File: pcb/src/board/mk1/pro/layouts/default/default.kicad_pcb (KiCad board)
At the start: 2 copper layers, 256 parts

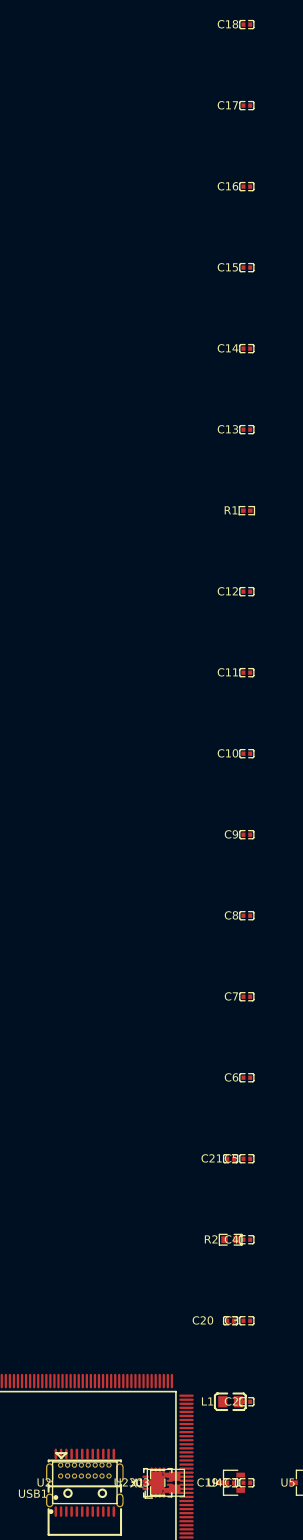
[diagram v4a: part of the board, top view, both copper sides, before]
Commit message: pcb: add decoupling capacitors to STM32F429
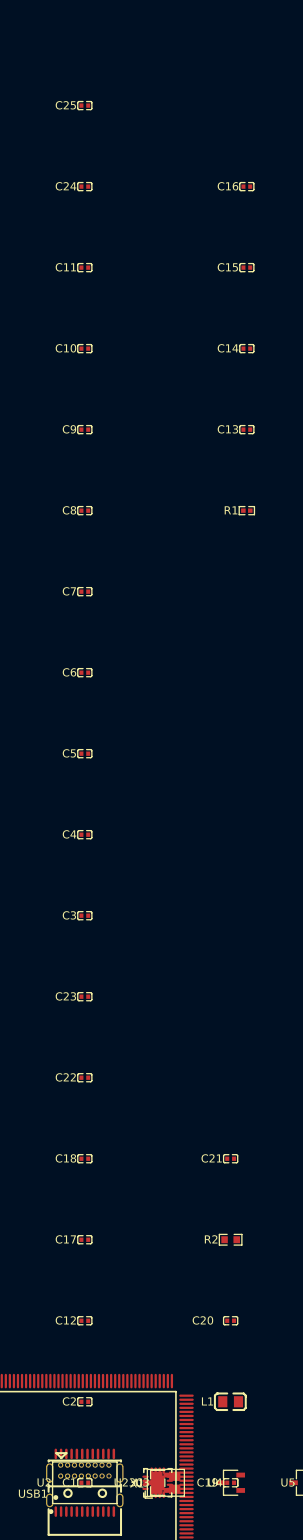
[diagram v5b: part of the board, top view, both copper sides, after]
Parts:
- added C22: 100nF ±10%, Samsung_Electro_Mechanics_CL05B104KO5NNNC:C0402, F.Cu at (0.00, -50.0)
- added C23: 100nF ±10%, Samsung_Electro_Mechanics_CL05B104KO5NNNC:C0402, F.Cu at (0.00, -60.0)
- added C24: 1µF ±10%, Samsung_Electro_Mechanics_CL05A105KA5NQNC:C0402, F.Cu at (0.00, -160.0)
- added C25: 10nF ±10%, Samsung_Electro_Mechanics_CL05B103KB5NNNC:C0402, F.Cu at (0.00, -170.0)
- C1: value 100nF ±10% -> 4.7µF ±20%; footprint Samsung_Electro_Mechanics_CL05B104KO5NNNC:C0402 -> Samsung_Electro_Mechanics_CL05A475MP5NRNC:C0402
- C17: value 1µF ±10% -> 100nF ±10%; footprint Samsung_Electro_Mechanics_CL05A105KA5NQNC:C0402 -> Samsung_Electro_Mechanics_CL05B104KO5NNNC:C0402
- moved C17 141.4 mm to (0.00, -30.0)
- moved C18 141.4 mm to (0.00, -40.0)
- moved C12 92.2 mm to (0.00, -20.0)
- moved C10 53.9 mm to (0.00, -140.0)
- moved C11 53.9 mm to (0.00, -150.0)
- moved C3 53.9 mm to (0.00, -70.0)
- moved C4 53.9 mm to (0.00, -80.0)
- moved C5 53.9 mm to (0.00, -90.0)
- moved C6 53.9 mm to (0.00, -100.0)
- moved C7 53.9 mm to (0.00, -110.0)
- moved C8 53.9 mm to (0.00, -120.0)
- moved C9 53.9 mm to (0.00, -130.0)
- moved C1 20.0 mm to (0.00, 0.00)
- moved C2 20.0 mm to (0.00, -10.0)
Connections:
- C1 pad 1: vref_caps[1]-power-hv -> out_cap-power-hv
- C10 pad 1: vref_caps[1]-power-hv -> out_cap-power-hv
- C11 pad 1: vref_caps[1]-power-hv -> out_cap-power-hv
- C12 pad 1: vref_caps[1]-power-hv -> out_cap-power-hv
- C15 pad 1: vcap_caps[1]-power-hv -> vcap_caps[0]-power-hv
- C17 pad 1: vref_caps[1]-power-hv -> out_cap-power-hv
- C18 pad 1: vref_caps[1]-power-hv -> out_cap-power-hv
- C2 pad 1: vref_caps[1]-power-hv -> out_cap-power-hv
- C20 pad 1: vref_caps[1]-power-hv -> out_cap-power-hv
- C3 pad 1: vref_caps[1]-power-hv -> out_cap-power-hv
- C4 pad 1: vref_caps[1]-power-hv -> out_cap-power-hv
- C5 pad 1: vref_caps[1]-power-hv -> out_cap-power-hv
- C6 pad 1: vref_caps[1]-power-hv -> out_cap-power-hv
- C7 pad 1: vref_caps[1]-power-hv -> out_cap-power-hv
- C8 pad 1: vref_caps[1]-power-hv -> out_cap-power-hv
- C9 pad 1: vref_caps[1]-power-hv -> out_cap-power-hv
- L1 pad 2: vref_caps[1]-power-hv -> out_cap-power-hv
- R2 pad 1: vref_caps[1]-power-hv -> out_cap-power-hv
- U1 pad 103: vref_caps[1]-power-hv -> out_cap-power-hv
- U1 pad 114: vref_caps[1]-power-hv -> out_cap-power-hv
- U1 pad 125: 125 -> vcap_caps[1]-power-hv
- U1 pad 127: vref_caps[1]-power-hv -> out_cap-power-hv
- U1 pad 136: vref_caps[1]-power-hv -> out_cap-power-hv
- U1 pad 149: vref_caps[1]-power-hv -> out_cap-power-hv
- U1 pad 15: vref_caps[1]-power-hv -> out_cap-power-hv
- U1 pad 159: vref_caps[1]-power-hv -> out_cap-power-hv
- U1 pad 172: vref_caps[1]-power-hv -> out_cap-power-hv
- U1 pad 23: vref_caps[1]-power-hv -> out_cap-power-hv
- U1 pad 36: vref_caps[1]-power-hv -> out_cap-power-hv
- U1 pad 38: vref_caps[1]-power-hv -> out_cap-power-hv
- U1 pad 39: vref_caps[1]-power-hv -> out_cap-power-hv
- U1 pad 49: vref_caps[1]-power-hv -> out_cap-power-hv
- U1 pad 6: vbat-hv -> out_cap-power-hv
- U1 pad 62: vref_caps[1]-power-hv -> out_cap-power-hv
- U1 pad 72: vref_caps[1]-power-hv -> out_cap-power-hv
- U1 pad 81: vcap_caps[1]-power-hv -> vcap_caps[0]-power-hv
- U1 pad 82: vref_caps[1]-power-hv -> out_cap-power-hv
- U1 pad 91: vref_caps[1]-power-hv -> out_cap-power-hv
- U10 pad 1: vref_caps[1]-power-hv -> out_cap-power-hv
- U100 pad 1: vref_caps[1]-power-hv -> out_cap-power-hv
- U101 pad 1: vref_caps[1]-power-hv -> out_cap-power-hv
- U102 pad 1: vref_caps[1]-power-hv -> out_cap-power-hv
- U103 pad 1: vref_caps[1]-power-hv -> out_cap-power-hv
- U104 pad 1: vref_caps[1]-power-hv -> out_cap-power-hv
- U105 pad 1: vref_caps[1]-power-hv -> out_cap-power-hv
- U106 pad 1: vref_caps[1]-power-hv -> out_cap-power-hv
- U107 pad 1: vref_caps[1]-power-hv -> out_cap-power-hv
- U108 pad 1: vref_caps[1]-power-hv -> out_cap-power-hv
- U109 pad 1: vref_caps[1]-power-hv -> out_cap-power-hv
- U11 pad 1: vref_caps[1]-power-hv -> out_cap-power-hv
- U110 pad 24: vref_caps[1]-power-hv -> out_cap-power-hv
- U111 pad 1: vref_caps[1]-power-hv -> out_cap-power-hv
- U112 pad 1: vref_caps[1]-power-hv -> out_cap-power-hv
- U113 pad 1: vref_caps[1]-power-hv -> out_cap-power-hv
- U114 pad 1: vref_caps[1]-power-hv -> out_cap-power-hv
- U115 pad 1: vref_caps[1]-power-hv -> out_cap-power-hv
- U116 pad 1: vref_caps[1]-power-hv -> out_cap-power-hv
- U117 pad 1: vref_caps[1]-power-hv -> out_cap-power-hv
- U118 pad 1: vref_caps[1]-power-hv -> out_cap-power-hv
- U119 pad 1: vref_caps[1]-power-hv -> out_cap-power-hv
- U12 pad 1: vref_caps[1]-power-hv -> out_cap-power-hv
- U120 pad 1: vref_caps[1]-power-hv -> out_cap-power-hv
- U121 pad 1: vref_caps[1]-power-hv -> out_cap-power-hv
- U122 pad 24: vref_caps[1]-power-hv -> out_cap-power-hv
- U123 pad 1: vref_caps[1]-power-hv -> out_cap-power-hv
- U124 pad 1: vref_caps[1]-power-hv -> out_cap-power-hv
- U125 pad 1: vref_caps[1]-power-hv -> out_cap-power-hv
- U126 pad 1: vref_caps[1]-power-hv -> out_cap-power-hv
- U127 pad 1: vref_caps[1]-power-hv -> out_cap-power-hv
- U128 pad 1: vref_caps[1]-power-hv -> out_cap-power-hv
- U129 pad 1: vref_caps[1]-power-hv -> out_cap-power-hv
- U13 pad 1: vref_caps[1]-power-hv -> out_cap-power-hv
- U130 pad 1: vref_caps[1]-power-hv -> out_cap-power-hv
- U131 pad 1: vref_caps[1]-power-hv -> out_cap-power-hv
- U132 pad 1: vref_caps[1]-power-hv -> out_cap-power-hv
- U133 pad 1: vref_caps[1]-power-hv -> out_cap-power-hv
- U134 pad 24: vref_caps[1]-power-hv -> out_cap-power-hv
- U135 pad 1: vref_caps[1]-power-hv -> out_cap-power-hv
- U136 pad 1: vref_caps[1]-power-hv -> out_cap-power-hv
- U137 pad 1: vref_caps[1]-power-hv -> out_cap-power-hv
- U138 pad 1: vref_caps[1]-power-hv -> out_cap-power-hv
- U139 pad 1: vref_caps[1]-power-hv -> out_cap-power-hv
- U14 pad 24: vref_caps[1]-power-hv -> out_cap-power-hv
- U140 pad 1: vref_caps[1]-power-hv -> out_cap-power-hv
- U141 pad 1: vref_caps[1]-power-hv -> out_cap-power-hv
- U142 pad 1: vref_caps[1]-power-hv -> out_cap-power-hv
- U143 pad 1: vref_caps[1]-power-hv -> out_cap-power-hv
- U144 pad 1: vref_caps[1]-power-hv -> out_cap-power-hv
- U145 pad 1: vref_caps[1]-power-hv -> out_cap-power-hv
- U146 pad 24: vref_caps[1]-power-hv -> out_cap-power-hv
- U147 pad 1: vref_caps[1]-power-hv -> out_cap-power-hv
- U148 pad 1: vref_caps[1]-power-hv -> out_cap-power-hv
- U149 pad 1: vref_caps[1]-power-hv -> out_cap-power-hv
- U15 pad 1: vref_caps[1]-power-hv -> out_cap-power-hv
- U150 pad 1: vref_caps[1]-power-hv -> out_cap-power-hv
- U151 pad 1: vref_caps[1]-power-hv -> out_cap-power-hv
- U152 pad 1: vref_caps[1]-power-hv -> out_cap-power-hv
- U153 pad 1: vref_caps[1]-power-hv -> out_cap-power-hv
- U154 pad 1: vref_caps[1]-power-hv -> out_cap-power-hv
- U155 pad 1: vref_caps[1]-power-hv -> out_cap-power-hv
- U156 pad 1: vref_caps[1]-power-hv -> out_cap-power-hv
- U157 pad 1: vref_caps[1]-power-hv -> out_cap-power-hv
- U158 pad 24: vref_caps[1]-power-hv -> out_cap-power-hv
- U159 pad 1: vref_caps[1]-power-hv -> out_cap-power-hv
- U16 pad 1: vref_caps[1]-power-hv -> out_cap-power-hv
- U160 pad 1: vref_caps[1]-power-hv -> out_cap-power-hv
- U161 pad 1: vref_caps[1]-power-hv -> out_cap-power-hv
- U162 pad 1: vref_caps[1]-power-hv -> out_cap-power-hv
- U163 pad 1: vref_caps[1]-power-hv -> out_cap-power-hv
- U164 pad 1: vref_caps[1]-power-hv -> out_cap-power-hv
- U165 pad 1: vref_caps[1]-power-hv -> out_cap-power-hv
- U166 pad 1: vref_caps[1]-power-hv -> out_cap-power-hv
- U167 pad 1: vref_caps[1]-power-hv -> out_cap-power-hv
- U168 pad 1: vref_caps[1]-power-hv -> out_cap-power-hv
- U169 pad 1: vref_caps[1]-power-hv -> out_cap-power-hv
- U17 pad 1: vref_caps[1]-power-hv -> out_cap-power-hv
- U170 pad 24: vref_caps[1]-power-hv -> out_cap-power-hv
- U171 pad 1: vref_caps[1]-power-hv -> out_cap-power-hv
- U172 pad 1: vref_caps[1]-power-hv -> out_cap-power-hv
- U173 pad 1: vref_caps[1]-power-hv -> out_cap-power-hv
- U174 pad 1: vref_caps[1]-power-hv -> out_cap-power-hv
- U175 pad 1: vref_caps[1]-power-hv -> out_cap-power-hv
- U176 pad 1: vref_caps[1]-power-hv -> out_cap-power-hv
- U177 pad 1: vref_caps[1]-power-hv -> out_cap-power-hv
- U178 pad 1: vref_caps[1]-power-hv -> out_cap-power-hv
- U179 pad 1: vref_caps[1]-power-hv -> out_cap-power-hv
- U18 pad 1: vref_caps[1]-power-hv -> out_cap-power-hv
- U180 pad 1: vref_caps[1]-power-hv -> out_cap-power-hv
- U181 pad 1: vref_caps[1]-power-hv -> out_cap-power-hv
- U182 pad 24: vref_caps[1]-power-hv -> out_cap-power-hv
- U183 pad 1: vref_caps[1]-power-hv -> out_cap-power-hv
- U184 pad 1: vref_caps[1]-power-hv -> out_cap-power-hv
- U185 pad 1: vref_caps[1]-power-hv -> out_cap-power-hv
- U186 pad 1: vref_caps[1]-power-hv -> out_cap-power-hv
- U187 pad 1: vref_caps[1]-power-hv -> out_cap-power-hv
- U188 pad 1: vref_caps[1]-power-hv -> out_cap-power-hv
- U189 pad 1: vref_caps[1]-power-hv -> out_cap-power-hv
- U19 pad 1: vref_caps[1]-power-hv -> out_cap-power-hv
- U190 pad 1: vref_caps[1]-power-hv -> out_cap-power-hv
- U191 pad 1: vref_caps[1]-power-hv -> out_cap-power-hv
- U192 pad 1: vref_caps[1]-power-hv -> out_cap-power-hv
- U193 pad 1: vref_caps[1]-power-hv -> out_cap-power-hv
- U194 pad 24: vref_caps[1]-power-hv -> out_cap-power-hv
- U195 pad 1: vref_caps[1]-power-hv -> out_cap-power-hv
- U196 pad 1: vref_caps[1]-power-hv -> out_cap-power-hv
- U197 pad 1: vref_caps[1]-power-hv -> out_cap-power-hv
- U198 pad 1: vref_caps[1]-power-hv -> out_cap-power-hv
- U199 pad 1: vref_caps[1]-power-hv -> out_cap-power-hv
- U2 pad 24: vref_caps[1]-power-hv -> out_cap-power-hv
- U20 pad 1: vref_caps[1]-power-hv -> out_cap-power-hv
- U200 pad 1: vref_caps[1]-power-hv -> out_cap-power-hv
- U201 pad 1: vref_caps[1]-power-hv -> out_cap-power-hv
- U202 pad 1: vref_caps[1]-power-hv -> out_cap-power-hv
- U203 pad 1: vref_caps[1]-power-hv -> out_cap-power-hv
- U204 pad 1: vref_caps[1]-power-hv -> out_cap-power-hv
- U205 pad 1: vref_caps[1]-power-hv -> out_cap-power-hv
- U206 pad 24: vref_caps[1]-power-hv -> out_cap-power-hv
- U207 pad 1: vref_caps[1]-power-hv -> out_cap-power-hv
- U208 pad 1: vref_caps[1]-power-hv -> out_cap-power-hv
- U209 pad 1: vref_caps[1]-power-hv -> out_cap-power-hv
- U21 pad 1: vref_caps[1]-power-hv -> out_cap-power-hv
- U210 pad 1: vref_caps[1]-power-hv -> out_cap-power-hv
- U211 pad 1: vref_caps[1]-power-hv -> out_cap-power-hv
- U212 pad 1: vref_caps[1]-power-hv -> out_cap-power-hv
- U213 pad 1: vref_caps[1]-power-hv -> out_cap-power-hv
- U214 pad 1: vref_caps[1]-power-hv -> out_cap-power-hv
- U215 pad 1: vref_caps[1]-power-hv -> out_cap-power-hv
- U216 pad 1: vref_caps[1]-power-hv -> out_cap-power-hv
- U217 pad 1: vref_caps[1]-power-hv -> out_cap-power-hv
- U218 pad 24: vref_caps[1]-power-hv -> out_cap-power-hv
- U219 pad 1: vref_caps[1]-power-hv -> out_cap-power-hv
- U22 pad 1: vref_caps[1]-power-hv -> out_cap-power-hv
- U220 pad 1: vref_caps[1]-power-hv -> out_cap-power-hv
- U221 pad 1: vref_caps[1]-power-hv -> out_cap-power-hv
- U222 pad 1: vref_caps[1]-power-hv -> out_cap-power-hv
- U223 pad 1: vref_caps[1]-power-hv -> out_cap-power-hv
- U224 pad 1: vref_caps[1]-power-hv -> out_cap-power-hv
- U225 pad 1: vref_caps[1]-power-hv -> out_cap-power-hv
- U226 pad 1: vref_caps[1]-power-hv -> out_cap-power-hv
- U227 pad 1: vref_caps[1]-power-hv -> out_cap-power-hv
- U228 pad 1: vref_caps[1]-power-hv -> out_cap-power-hv
- U229 pad 1: vref_caps[1]-power-hv -> out_cap-power-hv
- U23 pad 1: vref_caps[1]-power-hv -> out_cap-power-hv
- U230 pad 14: vref_caps[1]-power-hv -> out_cap-power-hv
- U24 pad 1: vref_caps[1]-power-hv -> out_cap-power-hv
- U25 pad 1: vref_caps[1]-power-hv -> out_cap-power-hv
- U26 pad 24: vref_caps[1]-power-hv -> out_cap-power-hv
- U27 pad 1: vref_caps[1]-power-hv -> out_cap-power-hv
- U28 pad 1: vref_caps[1]-power-hv -> out_cap-power-hv
- U29 pad 1: vref_caps[1]-power-hv -> out_cap-power-hv
- U3 pad 1: vref_caps[1]-power-hv -> out_cap-power-hv
- U30 pad 1: vref_caps[1]-power-hv -> out_cap-power-hv
- U31 pad 1: vref_caps[1]-power-hv -> out_cap-power-hv
- U32 pad 1: vref_caps[1]-power-hv -> out_cap-power-hv
- U33 pad 1: vref_caps[1]-power-hv -> out_cap-power-hv
- U34 pad 1: vref_caps[1]-power-hv -> out_cap-power-hv
- U35 pad 1: vref_caps[1]-power-hv -> out_cap-power-hv
- U36 pad 1: vref_caps[1]-power-hv -> out_cap-power-hv
- U37 pad 1: vref_caps[1]-power-hv -> out_cap-power-hv
- U38 pad 24: vref_caps[1]-power-hv -> out_cap-power-hv
- U39 pad 1: vref_caps[1]-power-hv -> out_cap-power-hv
- U4 pad 1: vref_caps[1]-power-hv -> out_cap-power-hv
- U40 pad 1: vref_caps[1]-power-hv -> out_cap-power-hv
- U41 pad 1: vref_caps[1]-power-hv -> out_cap-power-hv
- U42 pad 1: vref_caps[1]-power-hv -> out_cap-power-hv
- U43 pad 1: vref_caps[1]-power-hv -> out_cap-power-hv
- U44 pad 1: vref_caps[1]-power-hv -> out_cap-power-hv
- U45 pad 1: vref_caps[1]-power-hv -> out_cap-power-hv
- U46 pad 1: vref_caps[1]-power-hv -> out_cap-power-hv
- U47 pad 1: vref_caps[1]-power-hv -> out_cap-power-hv
- U48 pad 1: vref_caps[1]-power-hv -> out_cap-power-hv
- U49 pad 1: vref_caps[1]-power-hv -> out_cap-power-hv
- U5 pad 1: vref_caps[1]-power-hv -> out_cap-power-hv
- U50 pad 24: vref_caps[1]-power-hv -> out_cap-power-hv
- U51 pad 1: vref_caps[1]-power-hv -> out_cap-power-hv
- U52 pad 1: vref_caps[1]-power-hv -> out_cap-power-hv
- U53 pad 1: vref_caps[1]-power-hv -> out_cap-power-hv
- U54 pad 1: vref_caps[1]-power-hv -> out_cap-power-hv
- U55 pad 1: vref_caps[1]-power-hv -> out_cap-power-hv
- U56 pad 1: vref_caps[1]-power-hv -> out_cap-power-hv
- U57 pad 1: vref_caps[1]-power-hv -> out_cap-power-hv
- U58 pad 1: vref_caps[1]-power-hv -> out_cap-power-hv
- U59 pad 1: vref_caps[1]-power-hv -> out_cap-power-hv
- U6 pad 1: vref_caps[1]-power-hv -> out_cap-power-hv
- U60 pad 1: vref_caps[1]-power-hv -> out_cap-power-hv
- U61 pad 1: vref_caps[1]-power-hv -> out_cap-power-hv
- U62 pad 24: vref_caps[1]-power-hv -> out_cap-power-hv
- U63 pad 1: vref_caps[1]-power-hv -> out_cap-power-hv
- U64 pad 1: vref_caps[1]-power-hv -> out_cap-power-hv
- U65 pad 1: vref_caps[1]-power-hv -> out_cap-power-hv
- U66 pad 1: vref_caps[1]-power-hv -> out_cap-power-hv
- U67 pad 1: vref_caps[1]-power-hv -> out_cap-power-hv
- U68 pad 1: vref_caps[1]-power-hv -> out_cap-power-hv
- U69 pad 1: vref_caps[1]-power-hv -> out_cap-power-hv
- U7 pad 1: vref_caps[1]-power-hv -> out_cap-power-hv
- U70 pad 1: vref_caps[1]-power-hv -> out_cap-power-hv
- U71 pad 1: vref_caps[1]-power-hv -> out_cap-power-hv
- U72 pad 1: vref_caps[1]-power-hv -> out_cap-power-hv
- U73 pad 1: vref_caps[1]-power-hv -> out_cap-power-hv
- U74 pad 24: vref_caps[1]-power-hv -> out_cap-power-hv
- U75 pad 1: vref_caps[1]-power-hv -> out_cap-power-hv
- U76 pad 1: vref_caps[1]-power-hv -> out_cap-power-hv
- U77 pad 1: vref_caps[1]-power-hv -> out_cap-power-hv
- U78 pad 1: vref_caps[1]-power-hv -> out_cap-power-hv
- U79 pad 1: vref_caps[1]-power-hv -> out_cap-power-hv
- U8 pad 1: vref_caps[1]-power-hv -> out_cap-power-hv
- U80 pad 1: vref_caps[1]-power-hv -> out_cap-power-hv
- U81 pad 1: vref_caps[1]-power-hv -> out_cap-power-hv
- U82 pad 1: vref_caps[1]-power-hv -> out_cap-power-hv
- U83 pad 1: vref_caps[1]-power-hv -> out_cap-power-hv
- U84 pad 1: vref_caps[1]-power-hv -> out_cap-power-hv
- U85 pad 1: vref_caps[1]-power-hv -> out_cap-power-hv
- U86 pad 24: vref_caps[1]-power-hv -> out_cap-power-hv
- U87 pad 1: vref_caps[1]-power-hv -> out_cap-power-hv
- U88 pad 1: vref_caps[1]-power-hv -> out_cap-power-hv
- U89 pad 1: vref_caps[1]-power-hv -> out_cap-power-hv
- U9 pad 1: vref_caps[1]-power-hv -> out_cap-power-hv
- U90 pad 1: vref_caps[1]-power-hv -> out_cap-power-hv
- U91 pad 1: vref_caps[1]-power-hv -> out_cap-power-hv
- U92 pad 1: vref_caps[1]-power-hv -> out_cap-power-hv
- U93 pad 1: vref_caps[1]-power-hv -> out_cap-power-hv
- U94 pad 1: vref_caps[1]-power-hv -> out_cap-power-hv
- U95 pad 1: vref_caps[1]-power-hv -> out_cap-power-hv
- U96 pad 1: vref_caps[1]-power-hv -> out_cap-power-hv
- U97 pad 1: vref_caps[1]-power-hv -> out_cap-power-hv
- U98 pad 24: vref_caps[1]-power-hv -> out_cap-power-hv
- U99 pad 1: vref_caps[1]-power-hv -> out_cap-power-hv
